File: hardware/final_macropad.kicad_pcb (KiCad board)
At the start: 4 copper layers, 91.2 x 120.5 mm, 69 parts, among them J2 2137160001, SW1 SW_Push, U1 ATmega32U4-A, U2 USBLC6-2SC6, U3 DM-OLED096-636, Y1 16MHz

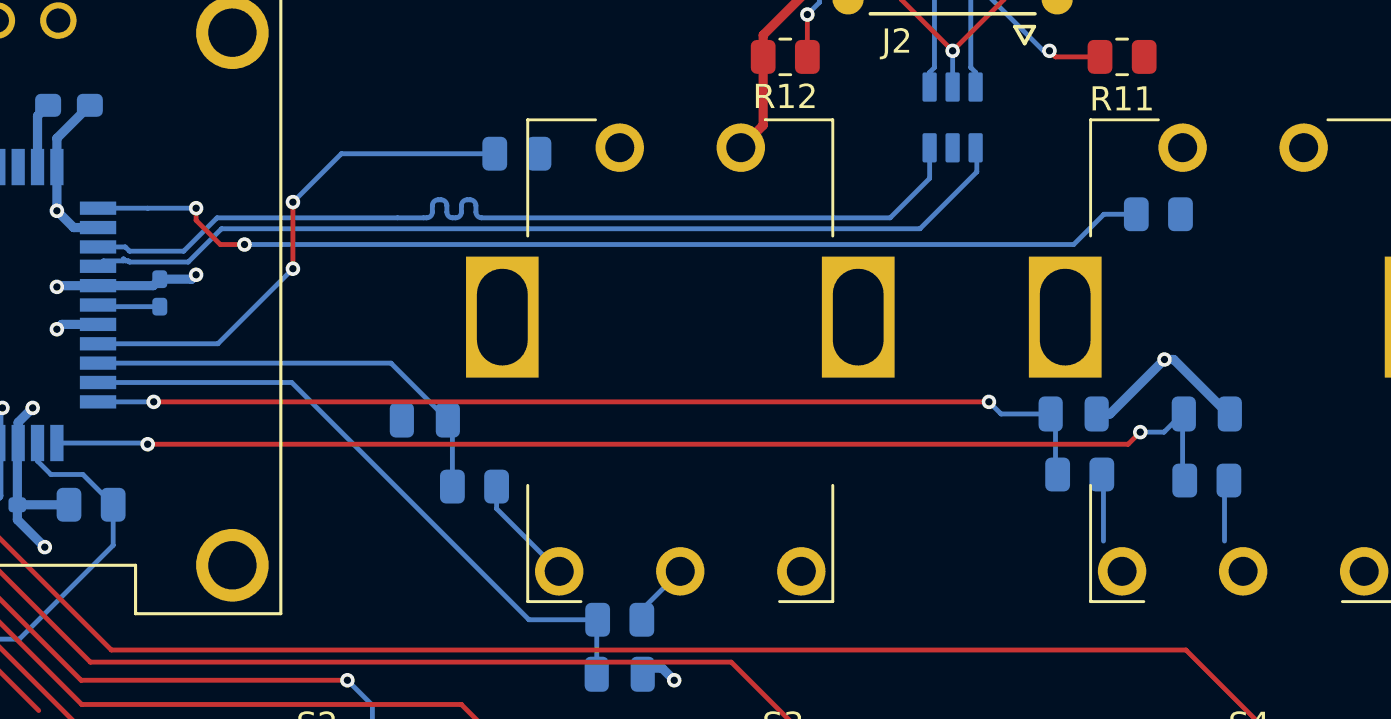
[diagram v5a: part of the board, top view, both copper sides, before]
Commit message: update PCB routing
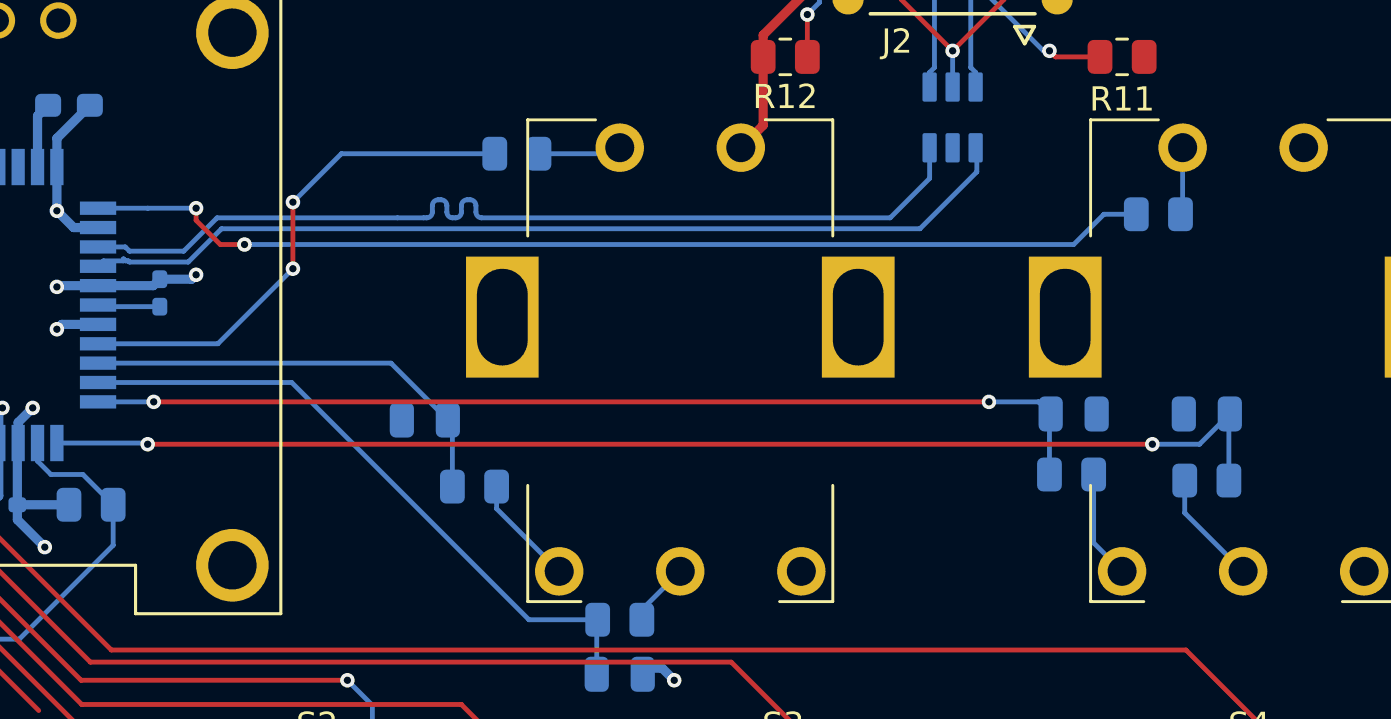
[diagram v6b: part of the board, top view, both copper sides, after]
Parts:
- moved R5 0.34 mm to (95.7, 51.2)
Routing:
- net ROTB0: track 59.4 -> 51.9 mm, vias 3 -> 2
- net Net-(S17-CHANNEL_B): track 0.00 -> 4.75 mm
- net Net-(R10-Pad2): track 0.00 -> 3.44 mm
- net Net-(R7-Pad2): track 0.00 -> 2.79 mm
- net Net-(S17-CHANNEL_A): track 2.81 -> 4.49 mm
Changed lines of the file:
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@@
 	(footprint "Resistor_SMD:R_0805_2012Metric"
 		(layer "B.Cu")
-		(at 96 51.25)
+		(at 95.6625 51.25)
 		(descr "Resistor SMD 0805 (2012 Metric), square (rectangular) end terminal, IPC-7351 nominal, (Body size source: IPC-SM-782 page 72, https://www.pcb-3d.com/wordpress/wp-content/uploads/ipc-sm-782a_amendment_1_and_2.pdf), generated with kicad-footprint-generator")
 		(tags "resistor")
@@
 	)
 	(segment
+		(start 100.25 40.4125)
+		(end 100.1625 40.5)
+		(width 0.2)
+		(layer "B.Cu")
+		(net 38)
+	)
+	(segment
+		(start 100.25 37.75)
+		(end 100.25 40.4125)
+		(width 0.2)
+		(layer "B.Cu")
+		(net 38)
+	)
+	(segment
 		(start 59.5 40.75)
 		(end 59.5 40.25)
@@
 	)
 	(segment
+		(start 76.75 38)
+		(end 77 37.75)
+		(width 0.2)
+		(layer "B.Cu")
+		(net 40)
+	)
+	(segment
+		(start 73.6625 38)
+		(end 76.75 38)
+		(width 0.2)
+		(layer "B.Cu")
+		(net 40)
+	)
+	(segment
 		(start 46.25 45)
 		(end 46.25 42.75)
@@
 	)
 	(segment
-		(start 92.75 48.75)
-		(end 95 48.75)
+		(start 94.75 48.8)
+		(end 94.8 48.75)
 		(width 0.2)
 		(layer "B.Cu")
@@
 	)
 	(segment
-		(start 92.25 48.25)
-		(end 92.75 48.75)
+		(start 94.75 51.25)
+		(end 94.75 48.8)
 		(width 0.2)
 		(layer "B.Cu")
@@
 	)
 	(segment
-		(start 95 51.25)
-		(end 95 48.75)
+		(start 94.3 48.25)
+		(end 92.25 48.25)
 		(width 0.2)
 		(layer "B.Cu")
@@
 	)
 	(segment
-		(start 98.5 49.5)
-		(end 98 50)
+		(start 94.8 48.75)
+		(end 94.3 48.25)
 		(width 0.2)
-		(layer "F.Cu")
-		(net 43)
+		(layer "B.Cu")
+		(net 42)
 	)
 	(segment
-		(start 98 50)
+		(start 99 50)
 		(end 57.5 50)
 		(width 0.2)
@@
 	)
 	(via
-		(at 99.5 46.5)
-		(size 0.6)
-		(drill 0.3)
-		(layers "F.Cu" "B.Cu")
-		(net 43)
-	)
-	(via
 		(at 57.5 50)
 		(size 0.6)
@@
 	)
 	(via
-		(at 98.5 49.5)
+		(at 99 50)
 		(size 0.6)
 		(drill 0.3)
@@
 	)
 	(segment
-		(start 99.8825 46.5)
-		(end 99.5 46.5)
-		(width 0.381)
-		(layer "B.Cu")
-		(net 43)
-	)
-	(segment
-		(start 101.981 54)
-		(end 101.981 51.344)
+		(start 100.95 50)
+		(end 102.2 48.75)
 		(width 0.2)
 		(layer "B.Cu")
@@
 	)
 	(segment
-		(start 102.1325 48.75)
-		(end 99.8825 46.5)
-		(width 0.381)
-		(layer "B.Cu")
-		(net 43)
-	)
-	(segment
-		(start 97.25 48.75)
-		(end 99.5 46.5)
-		(width 0.381)
-		(layer "B.Cu")
-		(net 43)
-	)
-	(segment
 		(start 57.45 49.95)
 		(end 53.75 49.95)
@@
 	)
 	(segment
-		(start 100.2325 48.75)
-		(end 99.4825 49.5)
-		(width 0.2)
-		(layer "B.Cu")
-		(net 43)
-	)
-	(segment
-		(start 100.25 51.25)
-		(end 100.25 48.7675)
-		(width 0.2)
-		(layer "B.Cu")
-		(net 43)
-	)
-	(segment
-		(start 99.4825 49.5)
-		(end 98.5 49.5)
+		(start 102.1625 51.5)
+		(end 102.1625 48.7875)
 		(width 0.2)
 		(layer "B.Cu")
@@
 	)
 	(segment
-		(start 96.9 48.75)
-		(end 97.25 48.75)
-		(width 0.381)
+		(start 99 50)
+		(end 100.95 50)
+		(width 0.2)
 		(layer "B.Cu")
 		(net 43)
 	)
 	(segment
-		(start 100.25 48.7675)
-		(end 100.2325 48.75)
+		(start 102.1625 48.7875)
+		(end 102.2 48.75)
 		(width 0.2)
 		(layer "B.Cu")
@@
 	)
 	(segment
-		(start 96.981 54)
-		(end 96.981 51.406)
+		(start 96.575 51.25)
+		(end 96.575 54.075)
 		(width 0.2)
 		(layer "B.Cu")
@@
 	)
 	(segment
-		(start 96.981 51.406)
-		(end 96.825 51.25)
+		(start 96.575 54.075)
+		(end 97.75 55.25)
 		(width 0.2)
 		(layer "B.Cu")
@@
 	)
 	(segment
+		(start 100.3375 51.5)
+		(end 100.3375 52.8375)
+		(width 0.2)
+		(layer "B.Cu")
+		(net 62)
+	)
+	(segment
+		(start 100.3375 52.8375)
+		(end 102.75 55.25)
+		(width 0.2)
+		(layer "B.Cu")
+		(net 62)
+	)
+	(segment

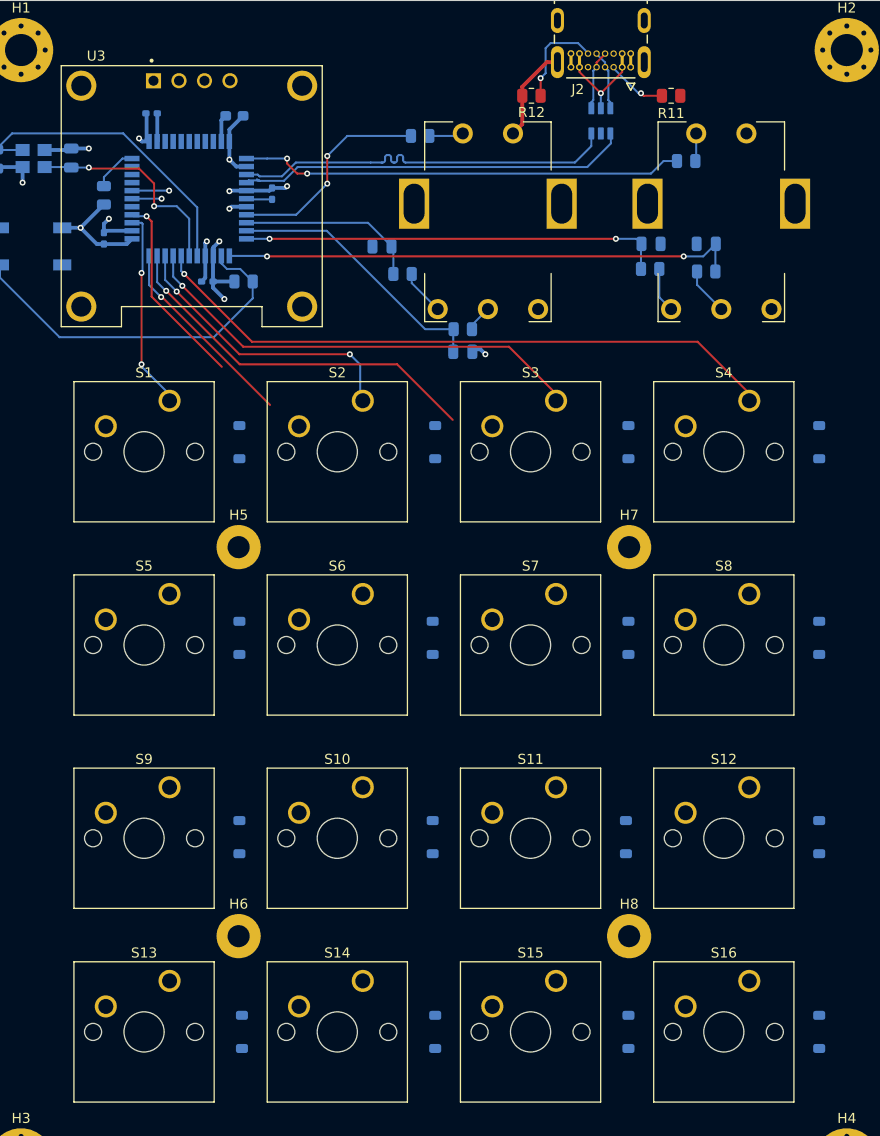
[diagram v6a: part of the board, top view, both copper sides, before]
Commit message: route all switches
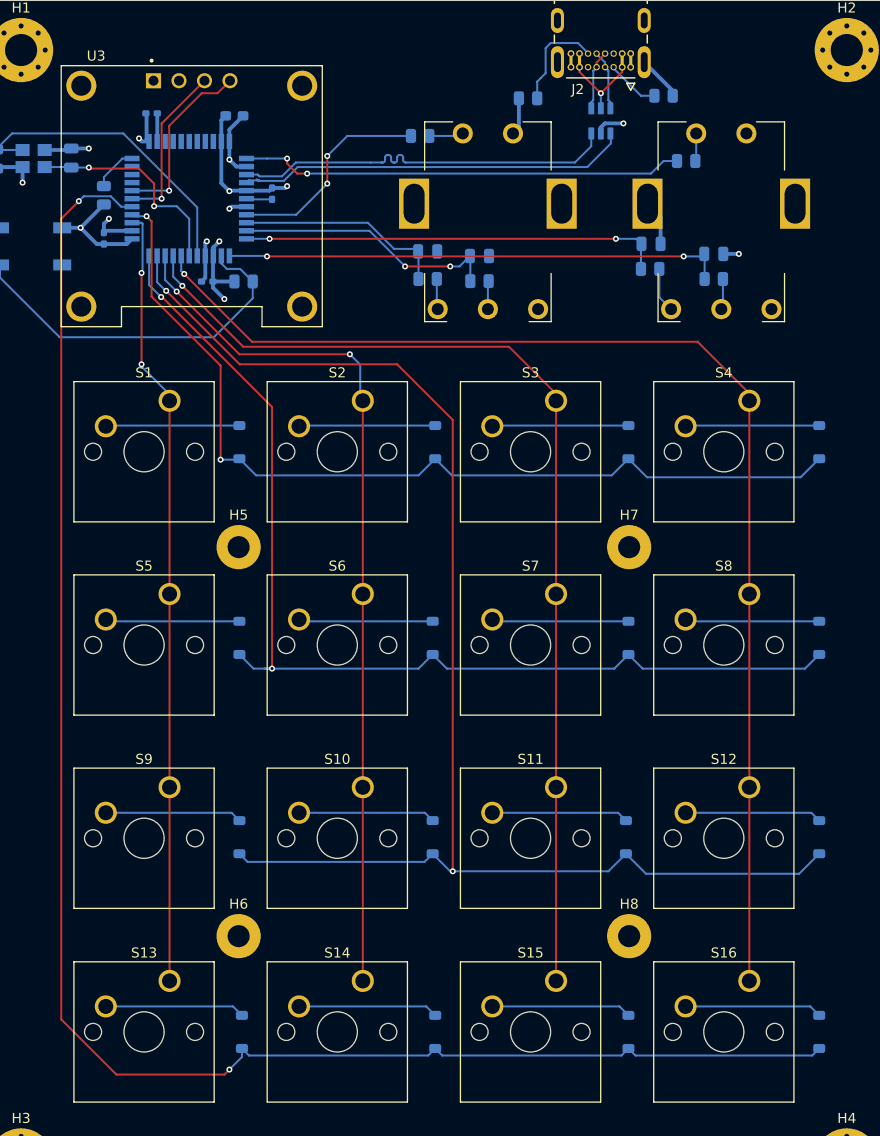
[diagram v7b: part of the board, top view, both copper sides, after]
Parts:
- R11, R12: moved to B.Cu
- moved C11 9.68 mm to (78.7, 50.0)
- moved R9 5.07 mm to (78.7, 52.5)
- moved C10 4.58 mm to (73.5, 49.5), turned to 0 degrees
- moved R8 2.55 mm to (73.5, 52.2)
- moved C9 1.25 mm to (102.0, 49.8), turned to 0 degrees
- moved R6 1.06 mm to (102.0, 52.2), turned to 0 degrees
- moved R11 0.75 mm to (97.0, 34.0)
- moved R12 0.42 mm to (83.5, 34.2)
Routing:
- net ROW 3: track 0.00 -> 169.3 mm, vias 0 -> 2
- net ROW 2: track 37.7 -> 144.2 mm, vias 1 -> 2
- net ROW 1: track 19.9 -> 108.2 mm, vias 1 -> 2
- net ROW 0: track 19.6 -> 92.8 mm, vias 1 -> 2
- net COL 0: track 18.9 -> 76.7 mm
- net COL 2: track 44.7 -> 102.5 mm
- net COL 1: track 28.0 -> 85.8 mm
- net COL 3: track 62.9 -> 120.7 mm
- net SDA: track 3.70 -> 18.1 mm
- net Net-(D15-A): track 0.00 -> 13.9 mm
- net Net-(D14-A): track 0.00 -> 13.9 mm
- net Net-(D13-A): track 0.00 -> 13.9 mm
- net Net-(D16-A): track 0.00 -> 13.7 mm
- net Net-(D7-A): track 0.00 -> 13.6 mm
- net Net-(D9-A): track 0.00 -> 13.6 mm
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
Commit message: check DRC
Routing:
- net GND: track 58.2 -> 75.7 mm, vias 8 -> 10
- net VBUS+: vias 2 -> 1
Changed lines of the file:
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@@
 			(layer "F.Fab")
 		)
-		(fp_text user "PTH Slot 1.6 +/- 0.05 X 0.7 +/- 0.05"
-			(at -0.5 2.25 0)
-			(layer "Dwgs.User")
-			(effects
-				(font
-					(size 0.393701 0.393701)
-					(thickness 0.15)
-				)
-			)
-		)
-		(fp_text user "PTH Slot 2.0 +/- 0.05 X 0.7 +/- 0.05"
-			(at -0.5 1.5 0)
-			(layer "Dwgs.User")
-			(effects
-				(font
-					(size 0.393701 0.393701)
-					(thickness 0.15)
-				)
-			)
-		)
 		(fp_text user "PCB Edge"
 			(at 5.5 -0.25 0)
@@
 		(tags "capacitor")
 		(property "Reference" "C6"
-			(at 0 1.68 90)
+			(at 2.55 0 0)
 			(layer "B.SilkS")
 			(effects
@@
 		(tags "capacitor")
 		(property "Reference" "C7"
-			(at 0 1.68 90)
+			(at -2.7 0.25 180)
 			(layer "B.SilkS")
 			(effects
@@
 		(tags "resistor")
 		(property "Reference" "R8"
-			(at 0 1.65 0)
+			(at -1.75 1.75 0)
 			(layer "B.SilkS")
 			(effects
@@
 		(tags "resistor")
 		(property "Reference" "R9"
-			(at -1.1625 1.65 0)
+			(at -1.4125 1.65 0)
 			(layer "B.SilkS")
 			(effects
@@
 		(tags "capacitor")
 		(property "Reference" "C10"
-			(at 1.75 -1.75 0)
+			(at 2.25 -1.5 0)
 			(layer "B.SilkS")
 			(effects
@@
 		(at 90.75 36.5 90)
 		(property "Reference" "U2"
-			(at 0.75 2.25 90)
+			(at 1 2.75 90)
 			(layer "B.SilkS")
 			(effects
 				(font
-					(size 0.64 0.64)
+					(size 0.8 0.64)
 					(thickness 0.15)
 				)
@@
 		(tags "resistor")
 		(property "Reference" "R6"
-			(at -1 1.5 0)
+			(at -1.5 1.75 0)
 			(layer "B.SilkS")
 			(effects
@@
 	)
 	(via
+		(at 46.262765 39.987235)
+		(size 0.6)
+		(drill 0.3)
+		(layers "F.Cu" "B.Cu")
+		(net 12)
+	)
+	(via
 		(at 38.925 47.15)
 		(size 0.6)
@@
 	)
 	(via
+		(at 75.5 46.5)
+		(size 0.6)
+		(drill 0.3)
+		(layers "F.Cu" "B.Cu")
+		(net 12)
+	)
+	(via
 		(at 104.5 49.75)
 		(size 0.6)
@@
 	)
 	(segment
+		(start 46.55 38.55)
+		(end 46.55 39.7)
+		(width 0.381)
+		(layer "B.Cu")
+		(net 12)
+	)
+	(segment
 		(start 40.5425 48.7675)
 		(end 38.925 47.15)
@@
 	)
 	(segment
+		(start 46.55 39.7)
+		(end 46.262765 39.987235)
+		(width 0.381)
+		(layer "B.Cu")
+		(net 12)
+	)
+	(segment
 		(start 41.25 48.7675)
 		(end 40.5425 48.7675)
@@
 	)
 	(segment
+		(start 46.5675 35.75)
+		(end 46.5675 32.8775)
+		(width 0.381)
+		(layer "B.Cu")
+		(net 12)
+	)
+	(segment
+		(start 74.45 47.25)
+		(end 74.45 47.05)
+		(width 0.381)
+		(layer "B.Cu")
+		(net 12)
+	)
+	(segment
 		(start 33.15 42.65)
 		(end 33.15 41.1)
@@
 	)
 	(segment
+		(start 75.5 46.5)
+		(end 76.15 46.5)
+		(width 0.381)
+		(layer "B.Cu")
+		(net 12)
+	)
+	(segment
 		(start 96.7 48.75)
 		(end 96.7 46.05)
@@
 	)
 	(segment
+		(start 76.15 46.5)
+		(end 79.6125 49.9625)
+		(width 0.381)
+		(layer "B.Cu")
+		(net 12)
+	)
+	(segment
 		(start 44.05 48.25)
 		(end 43.5325 48.7675)
@@
 	)
 	(segment
+		(start 75 46.5)
+		(end 74.45 47.05)
+		(width 0.381)
+		(layer "B.Cu")
+		(net 12)
+	)
+	(segment
 		(start 35.35 39.4)
 		(end 37.85 39.4)
@@
 	)
 	(segment
+		(start 74.45 49.5)
+		(end 74.45 47.25)
+		(width 0.381)
+		(layer "B.Cu")
+		(net 12)
+	)
+	(segment
 		(start 33.15 41.1)
 		(end 30.65 41.1)
@@
 	)
 	(segment
+		(start 46.5675 32.8775)
+		(end 46.19 32.5)
+		(width 0.381)
+		(layer "B.Cu")
+		(net 12)
+	)
+	(segment
 		(start 37.1 47.15)
 		(end 38.925 47.15)
@@
 	)
 	(segment
+		(start 75.5 46.5)
+		(end 75 46.5)
+		(width 0.381)
+		(layer "B.Cu")
+		(net 12)
+	)
+	(segment
+		(start 74.45 47.05)
+		(end 72.15 44.75)
+		(width 0.381)
+		(layer "B.Cu")
+		(net 12)
+	)
+	(segment
 		(start 57.7325 43.45)
 		(end 58 43.1825)
@@
 	)
 	(segment
-		(start 92.875 31.625)
-		(end 92.875 31.15)
+		(start 88.625 31.15)
+		(end 88.625 31.625)
 		(width 0.2)
 		(layer "F.Cu")
@@
 	)
 	(segment
-		(start 88.625 31.15)
-		(end 88.625 31.625)
+		(start 92.875 31.625)
+		(end 92.875 31.15)
 		(width 0.2)
 		(layer "F.Cu")
@@
 	)
 	(via
-		(at 92.875 31.15)
-		(size 0.6)
-		(drill 0.3)
-		(layers "F.Cu" "B.Cu")
-		(net 47)
-	)
-	(via
 		(at 90.75 33.75)
 		(size 0.6)
@@
 			(pts
 				(xy 25 23) (xy 122.75 23) (xy 124 24.25) (xy 124 150.25) (xy 29.75 150.25) (xy 25 150.25) (xy 25 55.25)
-				(xy 25 23)
 			)
 		)
